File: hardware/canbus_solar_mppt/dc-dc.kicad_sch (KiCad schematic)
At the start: 59 parts, among them J1 SOLAR_IN, J2 BATT2, J3 BATT1, Q1 SIR164ADP, Q2 SIR164ADP, Q3 SiSS27DN, Q4 SiSS27DN, Q5 BSS123, Q6 BSS123, Q7 SiSS27DN, Q8 SiSS27DN, U2 LP4951C, U3 NCP5901B, U4 PAC1953-1

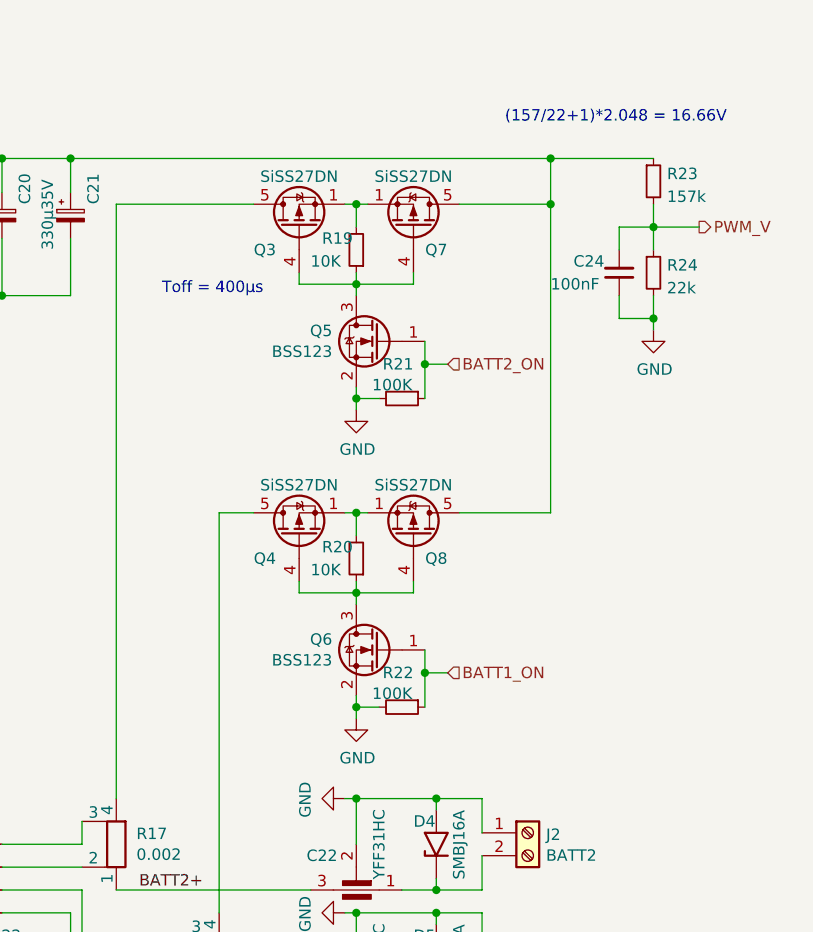
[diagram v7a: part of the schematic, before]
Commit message: Switch from BSS123 + GS resistor to DGD0215 mosfet driver.
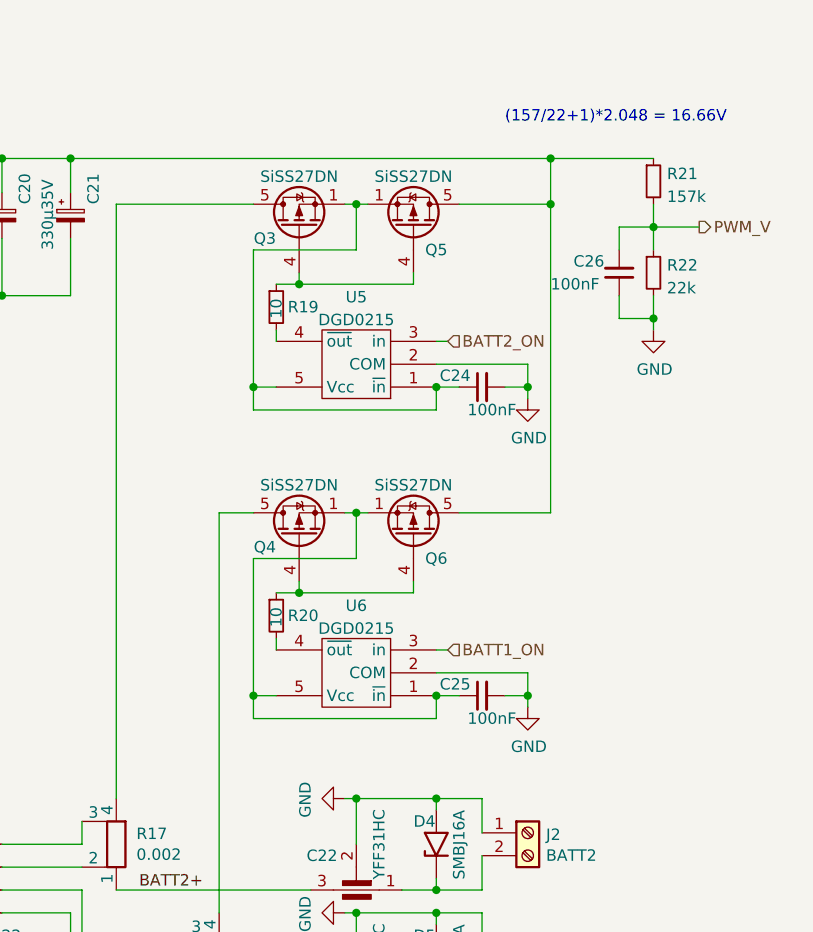
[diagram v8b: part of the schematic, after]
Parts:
- removed Q5, Q6: BSS123, Package_TO_SOT_SMD:SOT-23, symbol Device:Q_NMOS_GSD
- removed R21, R22: 100K, Resistor_SMD:R_0805_2012Metric_Pad1.20x1.40mm_HandSolder, symbol Device:R_Small
- added C24, C25: 100nF, Capacitor_SMD:C_1206_3216Metric_Pad1.33x1.80mm_HandSolder, symbol Device:C_Small
- added U5, U6: DGD0215, Package_TO_SOT_SMD:TSOT-23-5, symbol diode-local:DGD0215
- R19, R20: value 10K -> 10
- renumbered C24 to C26, Q7 to Q5, Q8 to Q6, R23 to R21, R24 to R22
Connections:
- net BATT1_ON: now also U6.3 (in)
- net BATT2_ON: now also U5.3 (in)
- net GND: now also C24.2, C25.2, U5.2 (COM), U6.2 (COM)
- net at Q3.1 (S), Q3.2 (S), Q3.3 (S)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: now also C24.1, U5.1 (~{in}), U5.5 (Vcc); no longer R19.2
- net at Q4.1 (S), Q4.2 (S), Q4.3 (S)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: now also C25.1, U6.1 (~{in}), U6.5 (Vcc); no longer R20.2
- new net: R19.2, U5.4 (~{out})
- new net: R20.2, U6.4 (~{out})
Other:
- note removed: "Toff = 400µs"
